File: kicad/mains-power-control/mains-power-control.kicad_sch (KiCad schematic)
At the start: 23 parts, among them J1 Conn_01x02_Socket, J2 Conn_01x03_Socket, J3 Conn_01x04_Pin, U1 BP, U2 SeeeduinoXIAO, U3 MOC3020M, U4 Optocoupler_DC_PhotoNPN_AKEC

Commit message: wip: pcb changes
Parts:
- removed D1, D2, D3, D5: BAV21, Diode_THT:D_DO-35_SOD27_P7.62mm_Horizontal, symbol Device:D_45deg
- removed H1: MountingHole, MountingHole:MountingHole_3.2mm_M3, symbol Mechanical:MountingHole
- removed J3: Conn_01x04_Pin, Connector_PinHeader_2.54mm:PinHeader_1x04_P2.54mm_Vertical, symbol Connector:Conn_01x04_Pin
- removed U4: Optocoupler_DC_PhotoNPN_AKEC, Package_DIP:DIP-4_W7.62mm, symbol Isolator:Optocoupler_DC_PhotoNPN_AKEC
- added J4: Conn_01x06_Pin, Connector_PinHeader_2.54mm:PinHeader_1x06_P2.54mm_Vertical, symbol Connector:Conn_01x06_Pin
- added U5: H11AA1, Package_DIP:DIP-6_W7.62mm, symbol Isolator:H11AA1
- J2: footprint Connector_Phoenix_MC_HighVoltage:PhoenixContact_MCV_1,5_3-G-5.08_1x03_P5.08mm_Vertical -> Connector_PinHeader_2.54mm:PinHeader_1x03_P2.54mm_Vertical
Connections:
- net 0V: now also J4.2 (Pin_2), U5.4
- net 5V: now also J4.1 (Pin_1)
- net L: now also R2.2
- net LED: now also J4.4 (Pin_4)
- net N: now also U5.2
- net SW: now also J4.3 (Pin_3)
- net Zero: now also U5.5
- net at R2.1: now also U5.1
- net SDA: now reaches U2.5 (PA06_D4_SDA)
- net SDA: now also J4.5 (Pin_5)
- net SCL: now reaches U2.6 (PA07_D5_SCL)
- net SCL: now also J4.6 (Pin_6)
- no-connect marks 33 -> 34

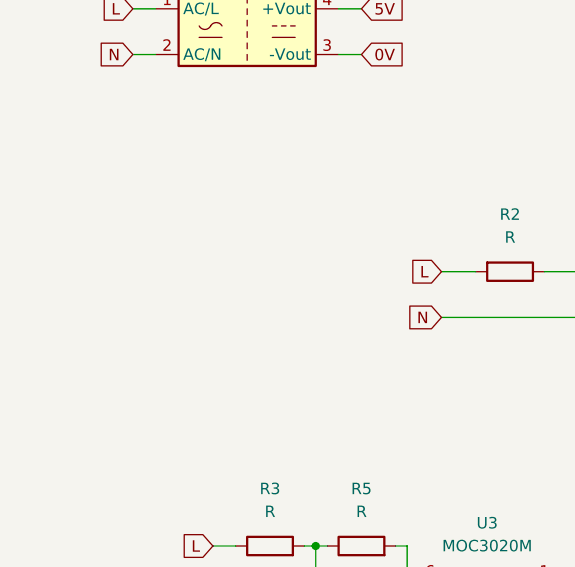
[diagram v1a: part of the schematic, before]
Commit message: Added UART socket to PCB
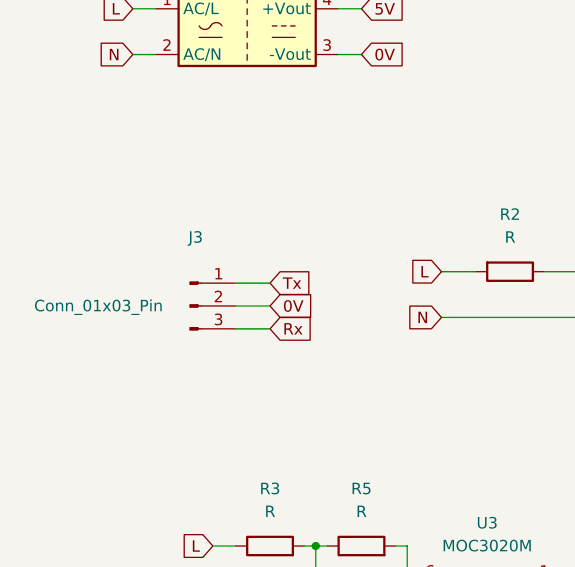
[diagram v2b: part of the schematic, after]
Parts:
- added J3: Conn_01x03_Pin, Connector_PinHeader_2.54mm:PinHeader_1x03_P2.54mm_Vertical, symbol Connector:Conn_01x03_Pin
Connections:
- net 0V: now also J3.2 (Pin_2)
- net Rx: now also J3.3 (Pin_3)
- net Tx: now also J3.1 (Pin_1)
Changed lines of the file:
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@@
+	(wire
+		(pts
+			(xy 52.07 67.31) (xy 55.88 67.31)
+		)
+		(stroke
+			(width 0)
+			(type default)
+		)
+	)
 	(wire
 		(pts
@@
 	(wire
 		(pts
+			(xy 52.07 72.39) (xy 55.88 72.39)
+		)
+		(stroke
+			(width 0)
+			(type default)
+		)
+	)
+	(wire
+		(pts
 			(xy 80.01 120.65) (xy 82.55 120.65)
 		)
@@
 	(wire
 		(pts
+			(xy 52.07 69.85) (xy 55.88 69.85)
+		)
+		(stroke
+			(width 0)
+			(type default)
+		)
+	)
+	(wire
+		(pts
 			(xy 121.92 110.49) (xy 124.46 110.49)
 		)
@@
 		)
 	)
+	(global_label "Rx"
+		(shape input)
+		(at 55.88 72.39 0)
+		(fields_autoplaced yes)
+		(effects
+			(font
+				(size 1.27 1.27)
+			)
+			(justify left)
+		)
+		(property "Intersheetrefs" "${INTERSHEET_REFS}"
+			(at 61.1633 72.39 0)
+			(effects
+				(font
+					(size 1.27 1.27)
+				)
+				(justify left)
+				(hide yes)
+			)
+		)
+	)
 	(global_label "L"
 		(shape input)
@@
 		)
 	)
+	(global_label "0V"
+		(shape input)
+		(at 55.88 69.85 0)
+		(fields_autoplaced yes)
+		(effects
+			(font
+				(size 1.27 1.27)
+			)
+			(justify left)
+		)
+		(property "Intersheetrefs" "${INTERSHEET_REFS}"
+			(at 61.1633 69.85 0)
+			(effects
+				(font
+					(size 1.27 1.27)
+				)
+				(justify left)
+				(hide yes)
+			)
+		)
+	)
 	(global_label "Tx"
 		(shape input)
@@
 		(property "Intersheetrefs" "${INTERSHEET_REFS}"
 			(at 143.51 72.2472 90)
+			(effects
+				(font
+					(size 1.27 1.27)
+				)
+				(justify left)
+				(hide yes)
+			)
+		)
+	)
+	(global_label "Tx"
+		(shape input)
+		(at 55.88 67.31 0)
+		(fields_autoplaced yes)
+		(effects
+			(font
+				(size 1.27 1.27)
+			)
+			(justify left)
+		)
+		(property "Intersheetrefs" "${INTERSHEET_REFS}"
+			(at 60.8609 67.31 0)
 			(effects
 				(font
@@
 					(unit 1)
 				)
+			)
+		)
+	)
+	(symbol
+		(lib_id "Connector:Conn_01x03_Pin")
+		(at 46.99 69.85 0)
+		(unit 1)
+		(exclude_from_sim no)
+		(in_bom yes)
+		(on_board yes)
+		(dnp no)
+		(property "Reference" "J3"
+			(at 47.625 62.23 0)
+			(effects
+				(font
+					(size 1.27 1.27)
+				)
+			)
+		)
+		(property "Value" "Conn_01x03_Pin"
+			(at 36.83 69.85 0)
+			(effects
+				(font
+					(size 1.27 1.27)
+				)
+			)
+		)
+		(property "Footprint" "Connector_PinHeader_2.54mm:PinHeader_1x03_P2.54mm_Vertical"
+			(at 46.99 69.85 0)
+			(effects
+				(font
+					(size 1.27 1.27)
+				)
+				(hide yes)
+			)
+		)
+		(property "Datasheet" "~"
+			(at 46.99 69.85 0)
+			(effects
+				(font
+					(size 1.27 1.27)
+				)
+				(hide yes)
+			)
+		)
+		(property "Description" "Generic connector, single row, 01x03, script generated"
+			(at 46.99 69.85 0)
+			(effects
+				(font
+					(size 1.27 1.27)
+				)
+				(hide yes)
+			)
+		)
+		(pin "3"
+		)
+		(pin "2"
+		)
+		(pin "1"
+		)
+		(instances
+			(project ""
+				(path "/ef5d369c-2cce-4e32-8236-63587eb624d9"
+					(reference "J3")
+					(unit 1)
+				)

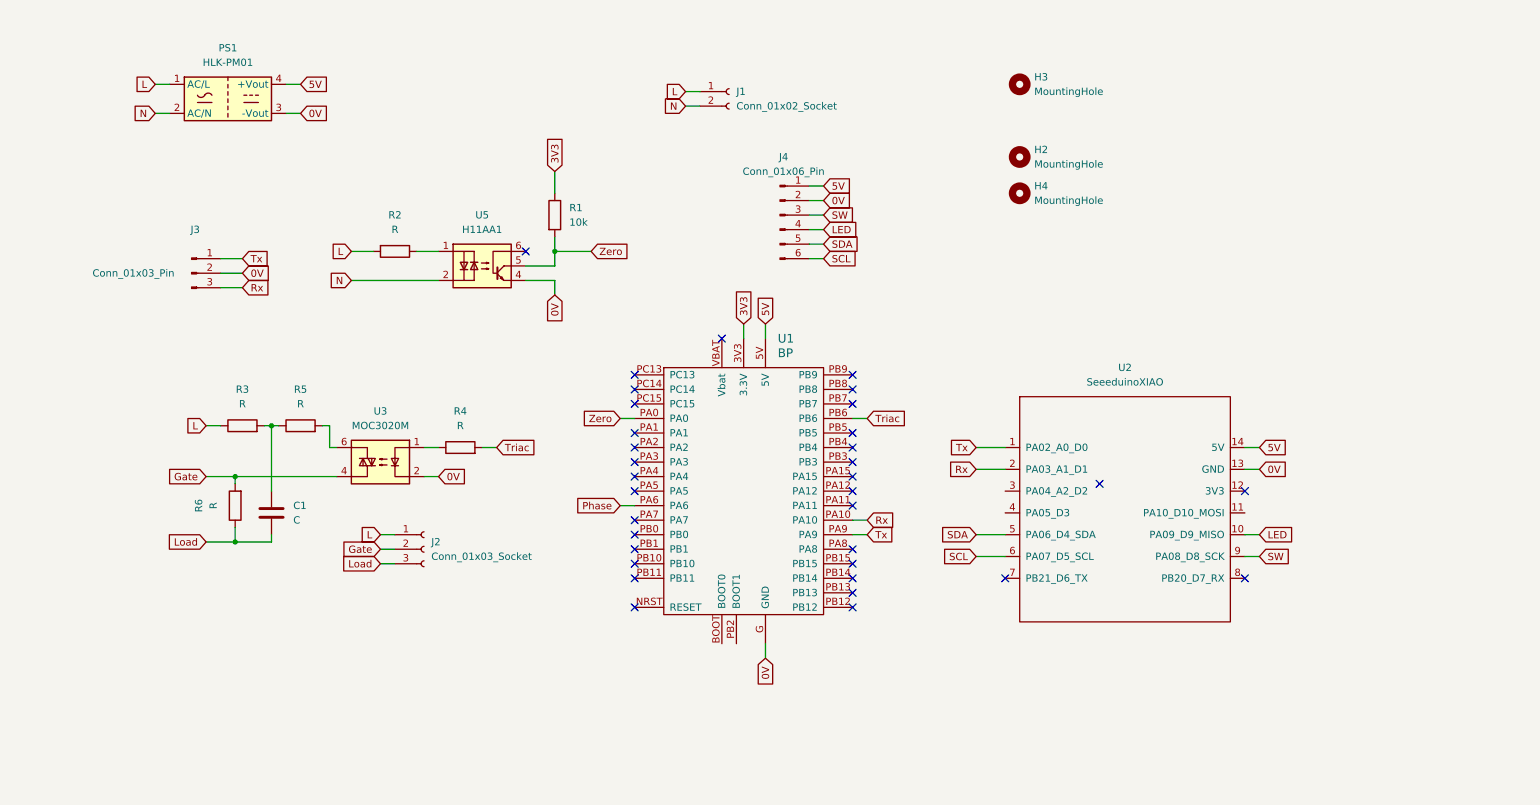
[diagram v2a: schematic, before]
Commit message: Added test points for STM32 timing signals
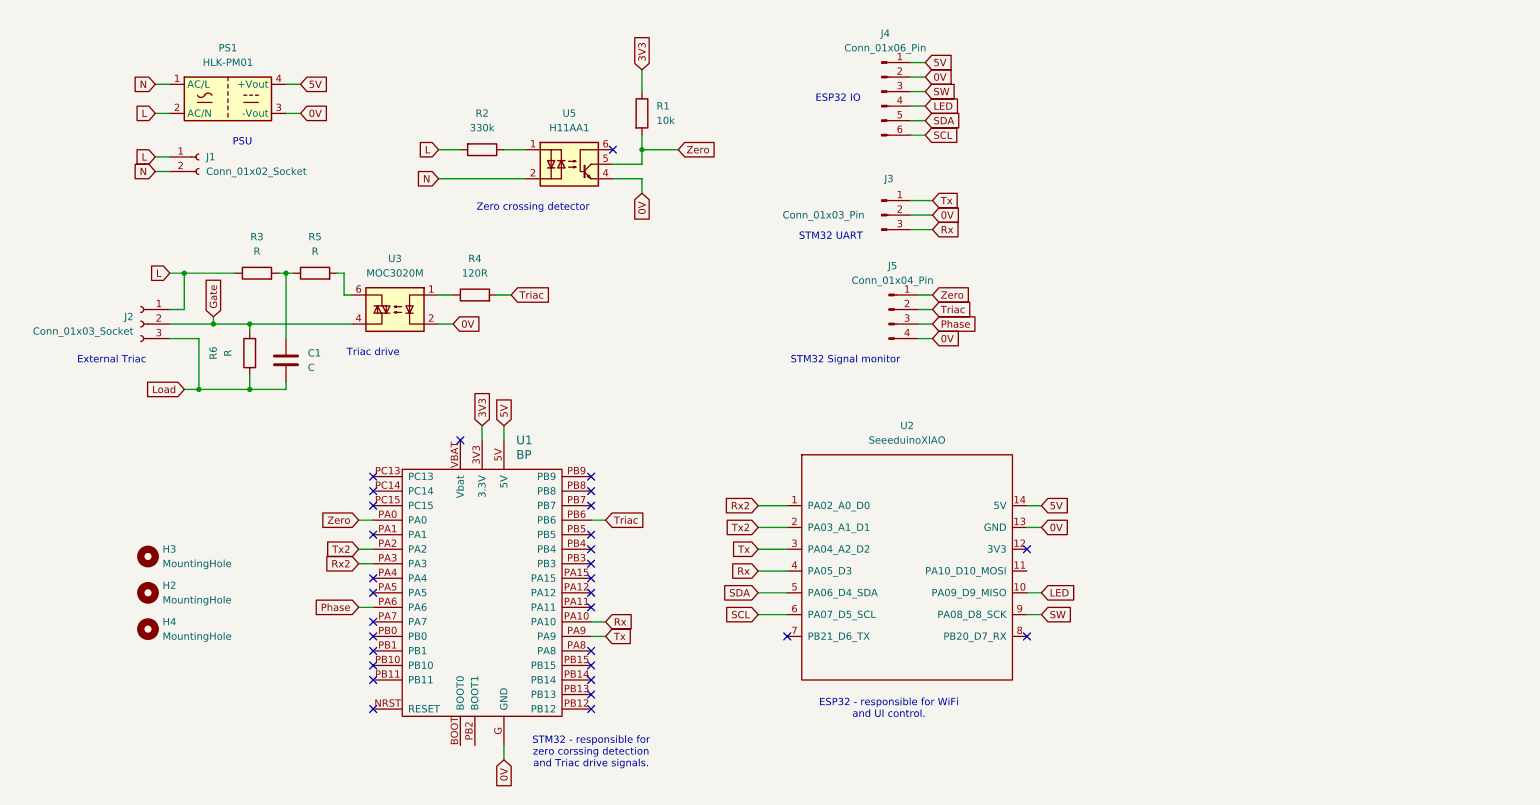
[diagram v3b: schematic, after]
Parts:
- added J5: Conn_01x04_Pin, Connector_PinHeader_2.54mm:PinHeader_1x04_P2.54mm_Vertical, symbol Connector:Conn_01x04_Pin
- R2: value R -> 330k
- R4: value R -> 120R
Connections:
- net 0V: now also J5.4 (Pin_4)
- net L: now also PS1.2 (AC/N); no longer PS1.1 (AC/L)
- net N: now also PS1.1 (AC/L); no longer PS1.2 (AC/N)
- net Phase: now also J5.3 (Pin_3)
- net Rx: now also U2.4 (PA05_D3); no longer U2.2 (PA03_A1_D1)
- net Triac: now also J5.2 (Pin_2)
- net Tx: now also U2.3 (PA04_A2_D2); no longer U2.1 (PA02_A0_D0)
- net Zero: now also J5.1 (Pin_1)
- net Tx2: now reaches U1.PA2
- net Tx2: now also U2.2 (PA03_A1_D1)
- net Rx2: now reaches U1.PA3
- net Rx2: now also U2.1 (PA02_A0_D0)
- no-connect marks 34 -> 31
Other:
- note added: "ESP32 - responsible for WiFi and UI control."
- note added: "ESP32 IO"
- note added: "External Triac"
- note added: "PSU"
- note added: "STM32 - responsible for zero corssing detection and Triac drive signals."
- note added: "STM32 Signal monitor"
- note added: "STM32 UART"
- note added: "Triac drive"
- note added: "Zero crossing detector"
- moved on the sheet: C1, H2, H3, H4, J1, J2, J3, J4, R1, R2, R3, R4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

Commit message: v 1.0 PCB release
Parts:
- added J6: Conn_01x02_Pin, Connector_PinHeader_2.54mm:PinHeader_1x02_P2.54mm_Vertical, symbol Connector:Conn_01x02_Pin
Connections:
- net 0V: now also J6.2 (Pin_2)
- net 3V3a: now reaches U2.12 (3V3)
- net 3V3a: now also J6.1 (Pin_1)
- no-connect marks 31 -> 30
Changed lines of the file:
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@@
-	)
-	(no_connect
-		(at 193.04 118.11)
 	)
 	(no_connect
@@
 	(wire
 		(pts
+			(xy 139.7 73.66) (xy 143.51 73.66)
+		)
+		(stroke
+			(width 0)
+			(type default)
+		)
+	)
+	(wire
+		(pts
 			(xy 125.73 34.29) (xy 125.73 38.1)
 		)
@@
 	(wire
 		(pts
+			(xy 193.04 118.11) (xy 195.58 118.11)
+		)
+		(stroke
+			(width 0)
+			(type default)
+		)
+	)
+	(wire
+		(pts
 			(xy 146.05 129.54) (xy 151.13 129.54)
 		)
@@
 	(wire
 		(pts
+			(xy 139.7 76.2) (xy 143.51 76.2)
+		)
+		(stroke
+			(width 0)
+			(type default)
+		)
+	)
+	(wire
+		(pts
 			(xy 173.99 81.28) (xy 176.53 81.28)
 		)
@@
 	(global_label "0V"
 		(shape input)
+		(at 143.51 76.2 0)
+		(fields_autoplaced yes)
+		(effects
+			(font
+				(size 1.27 1.27)
+			)
+			(justify left)
+		)
+		(property "Intersheetrefs" "${INTERSHEET_REFS}"
+			(at 148.7933 76.2 0)
+			(effects
+				(font
+					(size 1.27 1.27)
+				)
+				(justify left)
+				(hide yes)
+			)
+		)
+	)
+	(global_label "0V"
+		(shape input)
 		(at 92.71 78.74 0)
 		(fields_autoplaced yes)
@@
 		)
 	)
+	(global_label "3V3a"
+		(shape input)
+		(at 195.58 118.11 0)
+		(fields_autoplaced yes)
+		(effects
+			(font
+				(size 1.27 1.27)
+			)
+			(justify left)
+		)
+		(property "Intersheetrefs" "${INTERSHEET_REFS}"
+			(at 203.2218 118.11 0)
+			(effects
+				(font
+					(size 1.27 1.27)
+				)
+				(justify left)
+				(hide yes)
+			)
+		)
+	)
 	(global_label "0V"
 		(shape input)
@@
 				)
 				(justify right)
+				(hide yes)
+			)
+		)
+	)
+	(global_label "3V3a"
+		(shape input)
+		(at 143.51 73.66 0)
+		(fields_autoplaced yes)
+		(effects
+			(font
+				(size 1.27 1.27)
+			)
+			(justify left)
+		)
+		(property "Intersheetrefs" "${INTERSHEET_REFS}"
+			(at 151.1518 73.66 0)
+			(effects
+				(font
+					(size 1.27 1.27)
+				)
+				(justify left)
 				(hide yes)
 			)
@@
 					(unit 1)
 				)
+			)
+		)
+	)
+	(symbol
+		(lib_id "Connector:Conn_01x02_Pin")
+		(at 134.62 73.66 0)
+		(unit 1)
+		(exclude_from_sim no)
+		(in_bom yes)
+		(on_board yes)
+		(dnp no)
+		(fields_autoplaced yes)
+		(property "Reference" "J6"
+			(at 135.255 68.58 0)
+			(effects
+				(font
+					(size 1.27 1.27)
+				)
+			)
+		)
+		(property "Value" "Conn_01x02_Pin"
+			(at 135.255 71.12 0)
+			(effects
+				(font
+					(size 1.27 1.27)
+				)
+			)
+		)
+		(property "Footprint" "Connector_PinHeader_2.54mm:PinHeader_1x02_P2.54mm_Vertical"
+			(at 134.62 73.66 0)
+			(effects
+				(font
+					(size 1.27 1.27)
+				)
+				(hide yes)
+			)
+		)
+		(property "Datasheet" "~"
+			(at 134.62 73.66 0)
+			(effects
+				(font
+					(size 1.27 1.27)
+				)
+				(hide yes)
+			)
+		)
+		(property "Description" "Generic connector, single row, 01x02, script generated"
+			(at 134.62 73.66 0)
+			(effects
+				(font
+					(size 1.27 1.27)
+				)
+				(hide yes)
+			)
+		)
+		(pin "2"
+		)
+		(pin "1"
+		)
+		(instances
+			(project ""
+				(path "/ef5d369c-2cce-4e32-8236-63587eb624d9"
+					(reference "J6")
+					(unit 1)
+				)
